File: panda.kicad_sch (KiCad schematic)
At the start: 14 parts

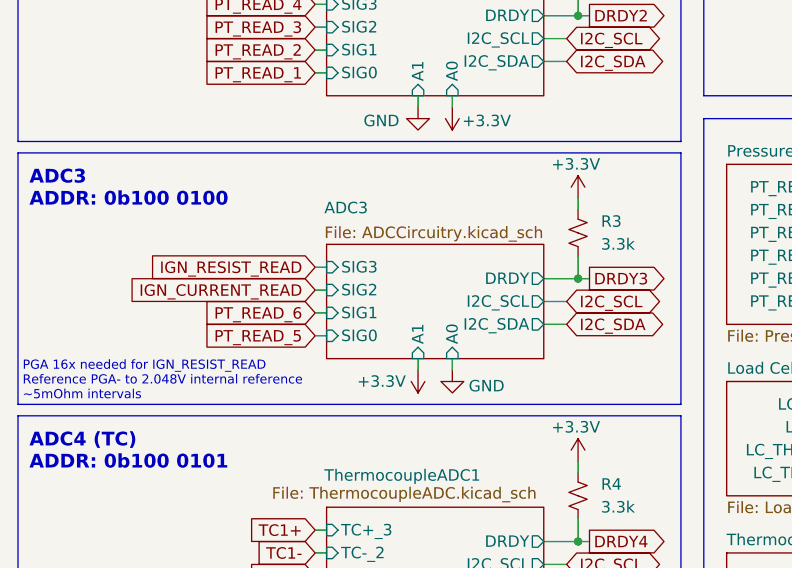
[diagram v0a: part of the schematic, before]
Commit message: fix ignitor resistance read circuit to use correct PGA reference
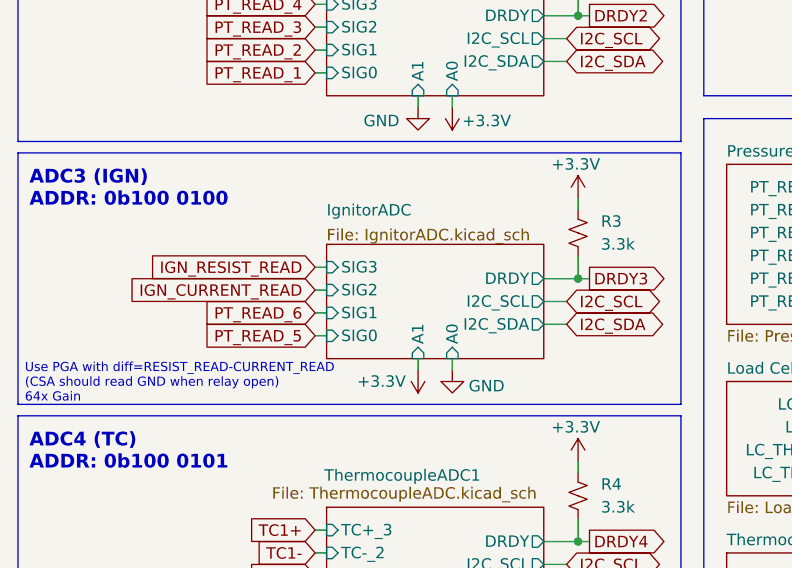
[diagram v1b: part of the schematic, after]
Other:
- removed sheet ADC3
- added sheet IgnitorADC (IgnitorADC.kicad_sch)
- note added: "ADC3 (IGN) ADDR: 0b100 0100"
- note added: "Use PGA with diff=RESIST_READ-CURRENT_READ (CSA should read GND when relay open) 64x Gain"
- note removed: "ADC3 ADDR: 0b100 0100"
- note removed: "PGA 16x needed for IGN_RESIST_READ Reference PGA- to 2.048V internal reference ~5mOhm intervals"
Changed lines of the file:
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@@
 		)
 	)
-	(text "ADC3\nADDR: 0b100 0100"
+	(text "ADC3 (IGN)\nADDR: 0b100 0100"
 		(exclude_from_sim no)
 		(at 15.24 80.264 0)
@@
 		)
 	)
-	(text "PGA 16x needed for IGN_RESIST_READ\nReference PGA- to 2.048V internal reference\n~5mOhm intervals"
+	(text "Use PGA with diff=RESIST_READ-CURRENT_READ\n(CSA should read GND when relay open)\n64x Gain"
 		(exclude_from_sim no)
-		(at 14.478 101.6 0)
+		(at 14.732 101.854 0)
 		(effects
 			(font
@@
 	)
 	(sheet
-		(at 48.26 86.36)
-		(size 24.13 12.7)
-		(exclude_from_sim no)
-		(in_bom yes)
-		(on_board yes)
-		(dnp no)
-		(stroke
-			(width 0.1524)
-			(type solid)
-		)
-		(fill
-			(color 0 0 0 0.0000)
-		)
-		(property "Sheetname" "ADC3"
-			(at 48.006 83.058 0)
-			(effects
-				(font
-					(size 1.27 1.27)
-				)
-				(justify left bottom)
-			)
-		)
-		(property "Sheetfile" "ADCCircuitry.kicad_sch"
-			(at 48.006 84.328 0)
-			(effects
-				(font
-					(size 1.27 1.27)
-				)
-				(justify left top)
-			)
-		)
-		(pin "A0" input
-			(at 62.23 99.06 270)
-			(effects
-				(font
-					(size 1.27 1.27)
-				)
-				(justify left)
-			)
-		)
-		(pin "A1" input
-			(at 58.42 99.06 270)
-			(effects
-				(font
-					(size 1.27 1.27)
-				)
-				(justify left)
-			)
-		)
-		(pin "DRDY" output
-			(at 72.39 90.17 0)
-			(effects
-				(font
-					(size 1.27 1.27)
-				)
-				(justify right)
-			)
-		)
-		(pin "SIG0" input
-			(at 48.26 96.52 180)
-			(effects
-				(font
-					(size 1.27 1.27)
-				)
-				(justify left)
-			)
-		)
-		(pin "SIG1" input
-			(at 48.26 93.98 180)
-			(effects
-				(font
-					(size 1.27 1.27)
-				)
-				(justify left)
-			)
-		)
-		(pin "SIG2" input
-			(at 48.26 91.44 180)
-			(effects
-				(font
-					(size 1.27 1.27)
-				)
-				(justify left)
-			)
-		)
-		(pin "SIG3" input
-			(at 48.26 88.9 180)
-			(effects
-				(font
-					(size 1.27 1.27)
-				)
-				(justify left)
-			)
-		)
-		(pin "I2C_SCL" output
-			(at 72.39 92.71 0)
-			(effects
-				(font
-					(size 1.27 1.27)
-				)
-				(justify right)
-			)
-		)
-		(pin "I2C_SDA" output
-			(at 72.39 95.25 0)
-			(effects
-				(font
-					(size 1.27 1.27)
-				)
-				(justify right)
-			)
-		)
-		(instances
-			(project "panda"
-				(path "/226c5870-4123-4efa-a2b3-b42d02f59bb7"
-					(page "6")
-				)
-			)
-		)
-	)
-	(sheet
 		(at 48.26 115.57)
 		(size 24.13 12.7)
@@
 				)
 			)
+		)
+	)
+	(sheet
+		(at 48.26 86.36)
+		(size 24.13 12.7)
+		(exclude_from_sim no)
+		(in_bom yes)
+		(on_board yes)
+		(dnp no)
+		(stroke
+			(width 0.1524)
+			(type solid)
+		)
+		(fill
+			(color 0 0 0 0.0000)
+		)
+		(property "Sheetname" "IgnitorADC"
+			(at 48.26 83.312 0)
+			(effects
+				(font
+					(size 1.27 1.27)
+				)
+				(justify left bottom)
+			)
+		)
+		(property "Sheetfile" "IgnitorADC.kicad_sch"
+			(at 48.26 84.582 0)
+			(effects
+				(font
+					(size 1.27 1.27)
+				)
+				(justify left top)
+			)
+		)
+		(pin "A0" input
+			(at 62.23 99.06 270)
+			(effects
+				(font
+					(size 1.27 1.27)
+				)
+				(justify left)
+			)
+		)
+		(pin "A1" input
+			(at 58.42 99.06 270)
+			(effects
+				(font
+					(size 1.27 1.27)
+				)
+				(justify left)
+			)
+		)
+		(pin "DRDY" output
+			(at 72.39 90.17 0)
+			(effects
+				(font
+					(size 1.27 1.27)
+				)
+				(justify right)
+			)
+		)
+		(pin "I2C_SCL" output
+			(at 72.39 92.71 0)
+			(effects
+				(font
+					(size 1.27 1.27)
+				)
+				(justify right)
+			)
+		)
+		(pin "I2C_SDA" output
+			(at 72.39 95.25 0)
+			(effects
+				(font
+					(size 1.27 1.27)
+				)
+				(justify right)
+			)
+		)
+		(pin "SIG0" input
+			(at 48.26 96.52 180)
+			(effects
+				(font
+					(size 1.27 1.27)
+				)
+				(justify left)
+			)
+		)
+		(pin "SIG1" input
+			(at 48.26 93.98 180)
+			(effects
+				(font
+					(size 1.27 1.27)
+				)
+				(justify left)
+			)
+		)
+		(pin "SIG2" input
+			(at 48.26 91.44 180)
+			(effects
+				(font
+					(size 1.27 1.27)
+				)
+				(justify left)
+			)
+		)
+		(pin "SIG3" input
+			(at 48.26 88.9 180)
+			(effects
+				(font
+					(size 1.27 1.27)
+				)
+				(justify left)
+			)
+		)
+		(instances
+			(project "panda"
+				(path "/226c5870-4123-4efa-a2b3-b42d02f59bb7"
+					(page "14")
+				)
+			)

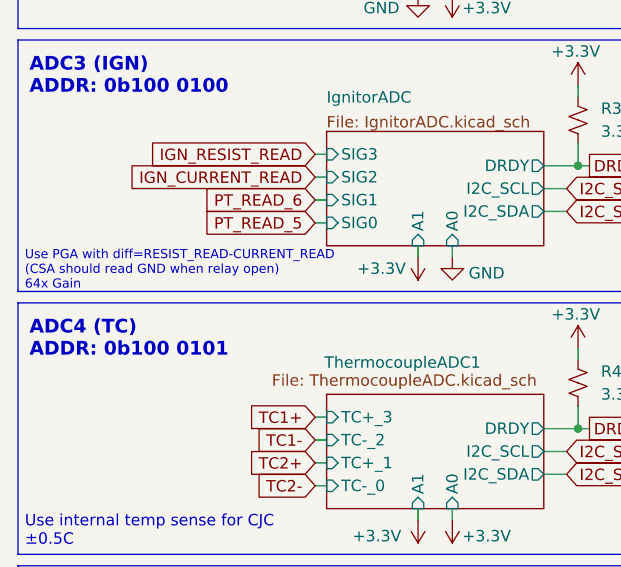
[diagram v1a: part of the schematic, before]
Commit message: add some comments to clarify ign_resist_read circuitry and implementation
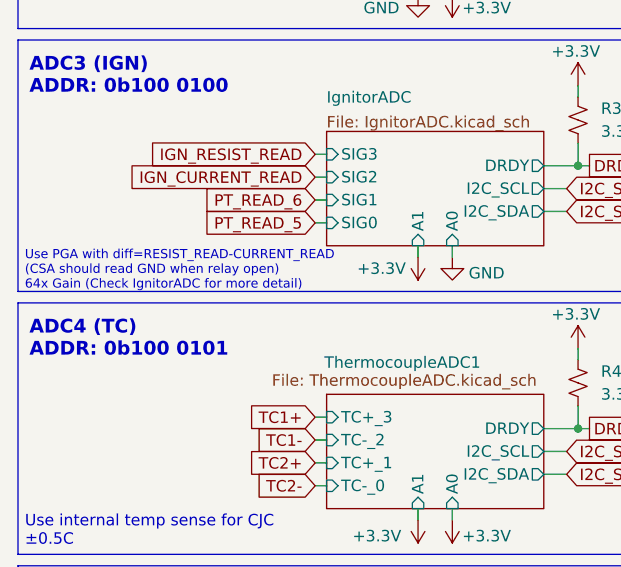
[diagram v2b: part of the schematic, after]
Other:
- note added: "Use PGA with diff=RESIST_READ-CURRENT_READ (CSA should read GND when relay open) 64x Gain (Check IgnitorADC for more detail)"
- note removed: "Use PGA with diff=RESIST_READ-CURRENT_READ (CSA should read GND when relay open) 64x Gain"
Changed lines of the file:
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@@
 		)
 	)
-	(text "Use PGA with diff=RESIST_READ-CURRENT_READ\n(CSA should read GND when relay open)\n64x Gain"
+	(text "Use PGA with diff=RESIST_READ-CURRENT_READ\n(CSA should read GND when relay open)\n64x Gain (Check IgnitorADC for more detail)"
 		(exclude_from_sim no)
 		(at 14.732 101.854 0)

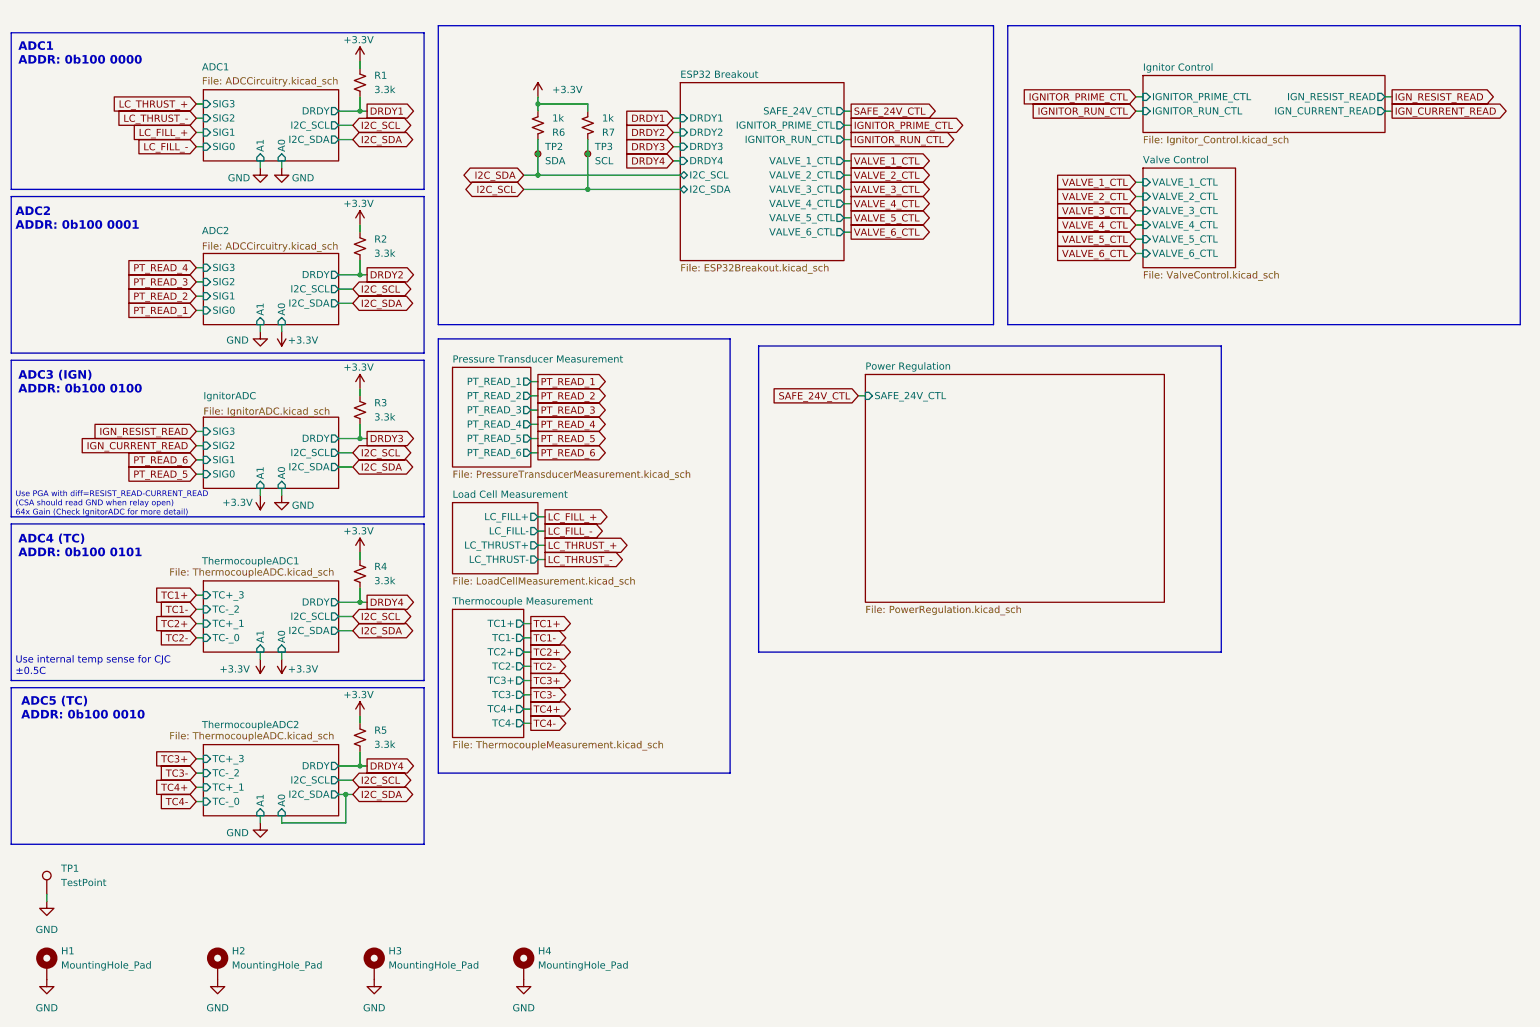
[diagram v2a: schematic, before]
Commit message: add capacitor and resistor footprints
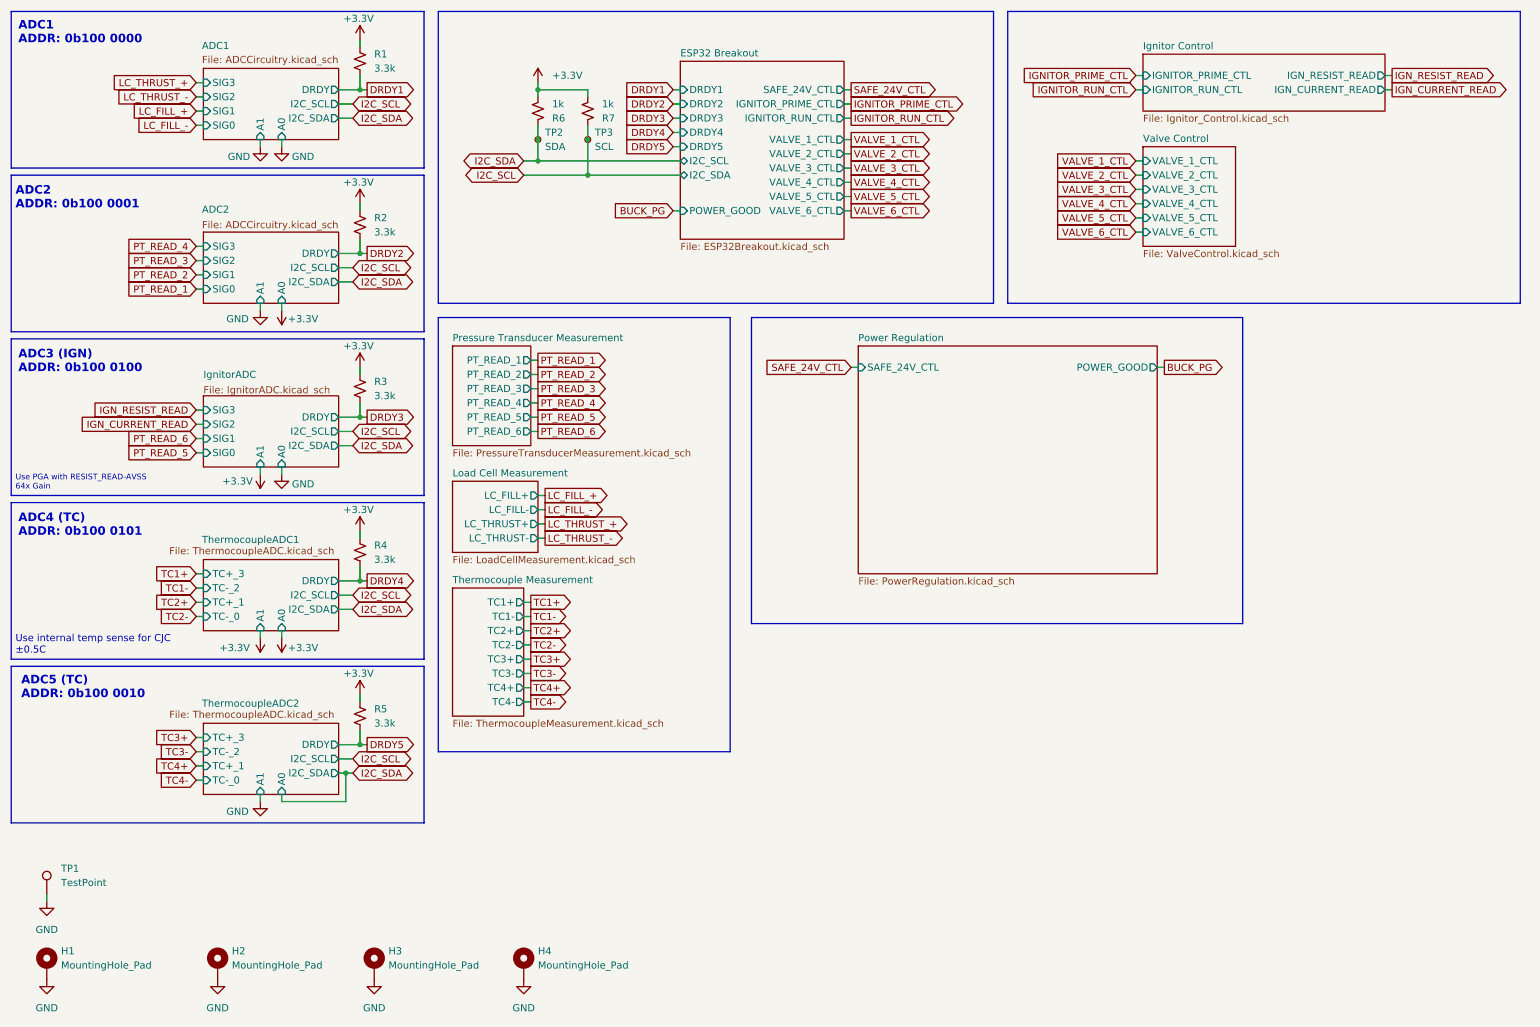
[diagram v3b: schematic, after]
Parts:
- R6, R7: LCSC (none) -> C11702
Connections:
- net DRDY4: no longer R5.2
- new net DRDY5: R5.2
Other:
- sheet ESP32 Breakout ports: added DRDY5, POWER_GOOD; removed none
- sheet Power Regulation ports: added POWER_GOOD; removed none
- note added: "Use PGA with RESIST_READ-AVSS 64x Gain"
- note removed: "Use PGA with diff=RESIST_READ-CURRENT_READ (CSA should read GND when relay open) 64x Gain (Check IgnitorADC for more detail)"
- moved on the sheet: R1, R2, R3, R4, R5, R6, R7, TP2, TP3

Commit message: change connectors and more progress on pcb
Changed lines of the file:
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@@
-	(wire
-		(pts
-			(xy 62.23 153.67) (xy 62.23 154.94)
-		)
-		(stroke
-			(width 0)
-			(type default)
-		)
-	)
 	(wire
 		(pts
@@
 	(wire
 		(pts
-			(xy 62.23 36.83) (xy 62.23 38.1)
-		)
-		(stroke
-			(width 0)
-			(type default)
-		)
-	)
-	(wire
-		(pts
 			(xy 73.66 149.86) (xy 74.93 149.86)
 		)
@@
 	(wire
 		(pts
-			(xy 62.23 66.04) (xy 62.23 67.31)
-		)
-		(stroke
-			(width 0)
-			(type default)
-		)
-	)
-	(wire
-		(pts
 			(xy 76.2 142.24) (xy 76.2 144.78)
 		)
@@
 	(wire
 		(pts
-			(xy 58.42 66.04) (xy 58.42 67.31)
-		)
-		(stroke
-			(width 0)
-			(type default)
-		)
-	)
-	(wire
-		(pts
 			(xy 46.99 121.92) (xy 48.26 121.92)
 		)
@@
 	(wire
 		(pts
-			(xy 58.42 36.83) (xy 58.42 38.1)
-		)
-		(stroke
-			(width 0)
-			(type default)
-		)
-	)
-	(wire
-		(pts
 			(xy 76.2 27.94) (xy 77.47 27.94)
 		)
@@
 	(wire
 		(pts
-			(xy 62.23 95.25) (xy 62.23 96.52)
-		)
-		(stroke
-			(width 0)
-			(type default)
-		)
-	)
-	(wire
-		(pts
 			(xy 46.99 119.38) (xy 48.26 119.38)
 		)
@@
 	(wire
 		(pts
-			(xy 58.42 95.25) (xy 58.42 96.52)
-		)
-		(stroke
-			(width 0)
-			(type default)
-		)
-	)
-	(wire
-		(pts
 			(xy 72.39 86.36) (xy 76.2 86.36)
 		)
@@
 	(wire
 		(pts
-			(xy 58.42 124.46) (xy 58.42 125.73)
-		)
-		(stroke
-			(width 0)
-			(type default)
-		)
-	)
-	(wire
-		(pts
-			(xy 58.42 153.67) (xy 58.42 154.94)
-		)
-		(stroke
-			(width 0)
-			(type default)
-		)
-	)
-	(wire
-		(pts
 			(xy 76.2 83.82) (xy 76.2 86.36)
 		)
@@
 		)
 		(stroke
-			(width 0)
-			(type default)
-		)
-	)
-	(wire
-		(pts
-			(xy 62.23 124.46) (xy 62.23 125.73)
-		)
-		(stroke
